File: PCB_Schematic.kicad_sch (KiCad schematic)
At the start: 64 parts, among them J1 IMU_1, J2 Power_Connector, J3 Programming Header, J4 Conn_01x02_Pin, J6 USB_A, J7 Ultrasonic, J8 IMU_2, Q7 BSS138, SW1 Reset Switch, U1 MAX7375AXR805, U2 LM1117MP-ADJ, U3 TPS54331-Q1, U5 FT232RL, U6 STM32F091RCTx

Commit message: minor footprint changes
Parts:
- J2: footprint (none) -> Library:CONN_B4B-XH-A_JSTProject
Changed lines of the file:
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@@
 			)
 		)
-		(property "Footprint" ""
+		(property "Footprint" "Library:CONN_B4B-XH-A_JSTProject"
 			(at 267.97 88.9 0)
 			(effects

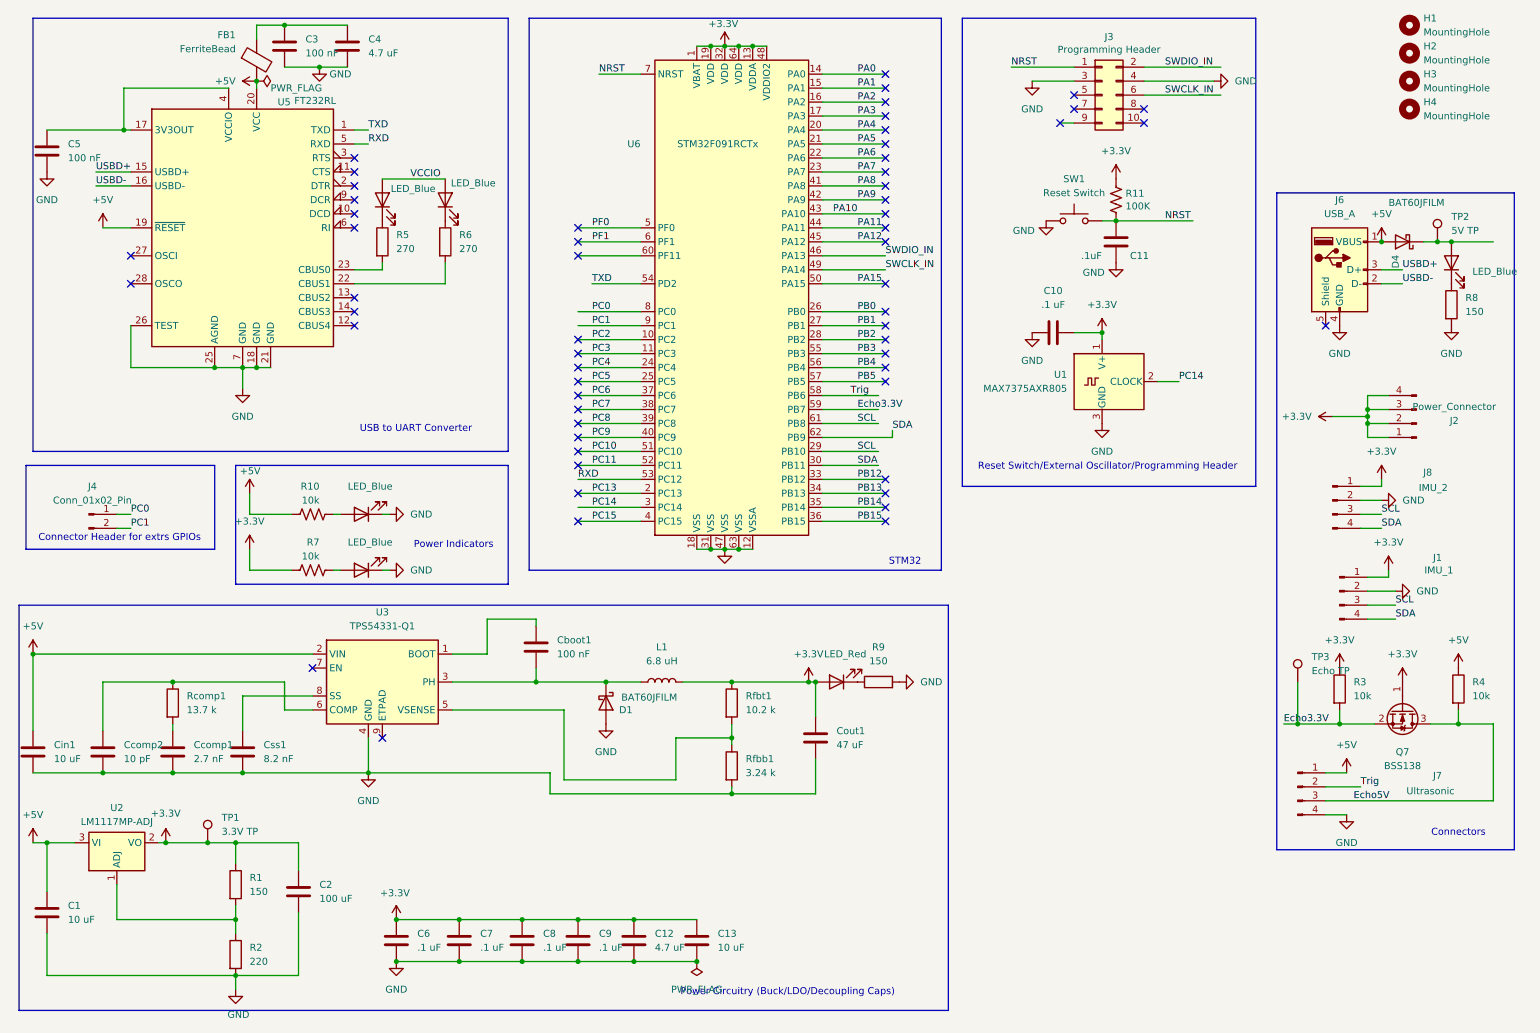
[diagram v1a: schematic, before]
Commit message: OSC_IN pin change, add BOOT0, just copy programming header from schematic
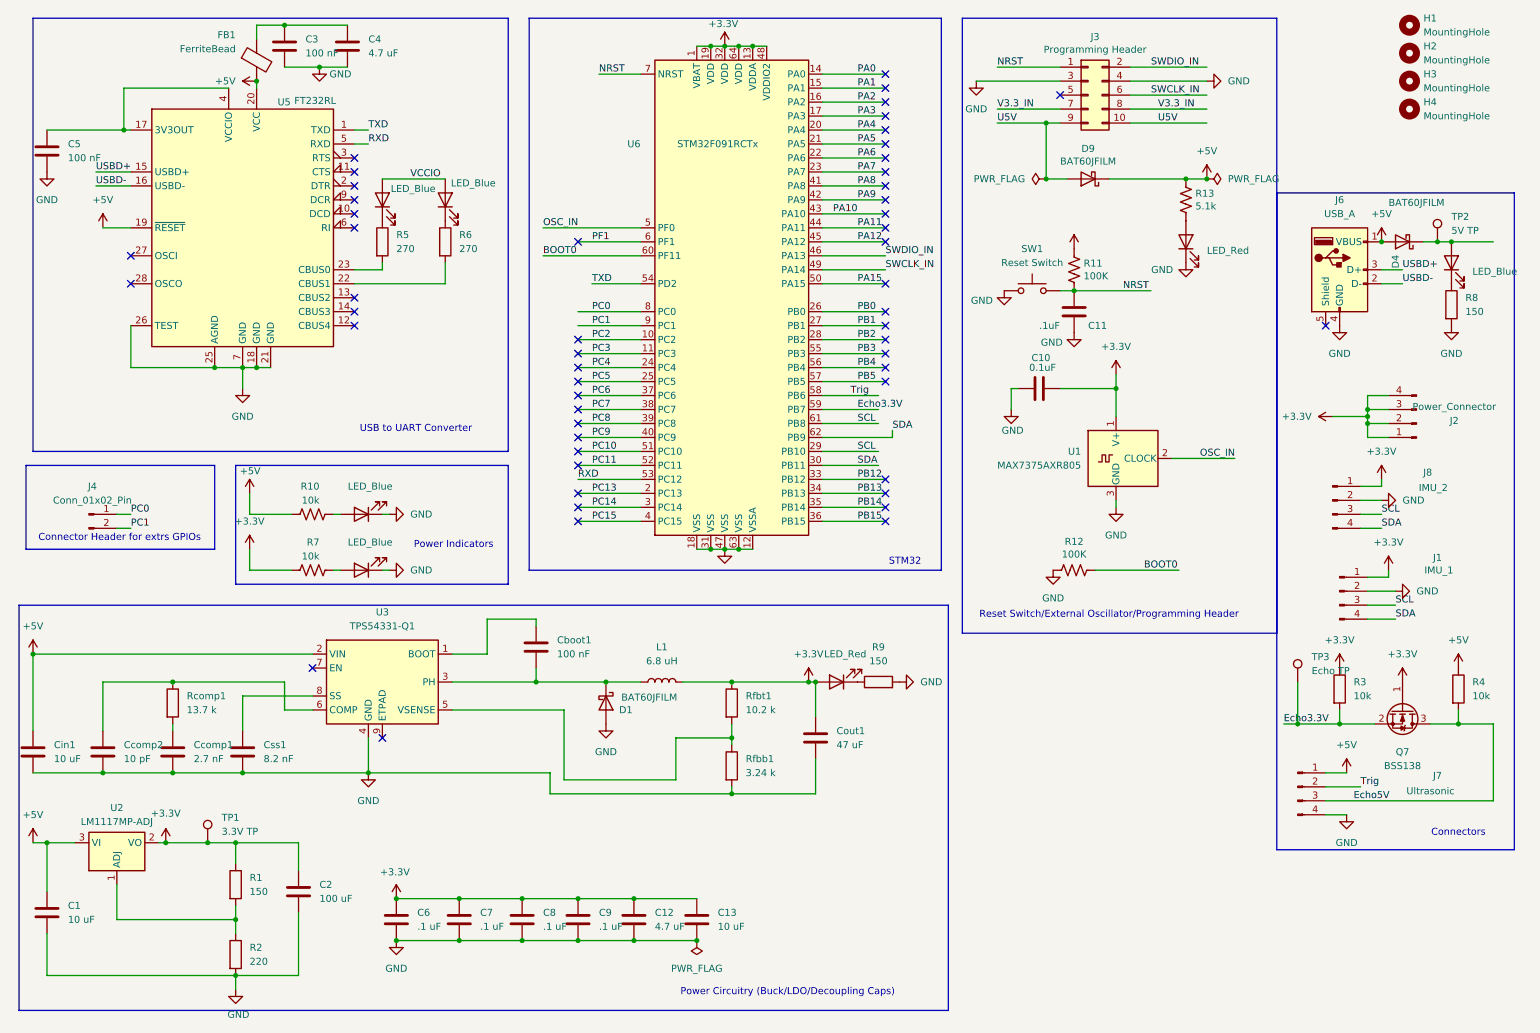
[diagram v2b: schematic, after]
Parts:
- added D10: LED_Red, LED_SMD:LED_0805_2012Metric_Pad1.15x1.40mm_HandSolder, symbol Device:LED
- added D9: BAT60JFILM, Diode_SMD:D_0805_2012Metric_Pad1.15x1.40mm_HandSolder, symbol Diode:BAT60A
- added R12: 100K, Resistor_SMD:R_0805_2012Metric_Pad1.20x1.40mm_HandSolder, symbol Device:R_US
- added R13: 5.1k, Resistor_SMD:R_0805_2012Metric_Pad1.20x1.40mm_HandSolder, symbol Device:R_US
- C10: value .1 uF -> 0.1uF
- U1: footprint Package_TO_SOT_SMD:SOT-323_SC-70 -> Package_TO_SOT_SMD:SOT-323_SC-70_Handsoldering
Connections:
- net +3.3V: now also C10.2; no longer C10.1
- net +5V: now also D9.1 (K), R13.1
- net GND: now also C10.1, D10.1 (K), R12.2; no longer C10.2
- net PC14: no longer U1.2 (CLOCK)
- net BOOT0: now reaches U6.60 (PF11)
- net BOOT0: now also R12.1
- net U5V: now reaches J3.10 (Pin_10)
- net U5V: now also J3.9 (Pin_9), D9.2 (A)
- net V3.3_IN: now reaches J3.7 (Pin_7)
- net V3.3_IN: now also J3.8 (Pin_8)
- net PF0 renamed OSC_IN
- net OSC_IN: now also U1.2 (CLOCK)
- new net: D10.2 (A), R13.2
- no-connect marks 58 -> 53
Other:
- moved on the sheet: C11, C12, C13, C6, C7, C8, C9, R11, SW1

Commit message: new ESD and footprints
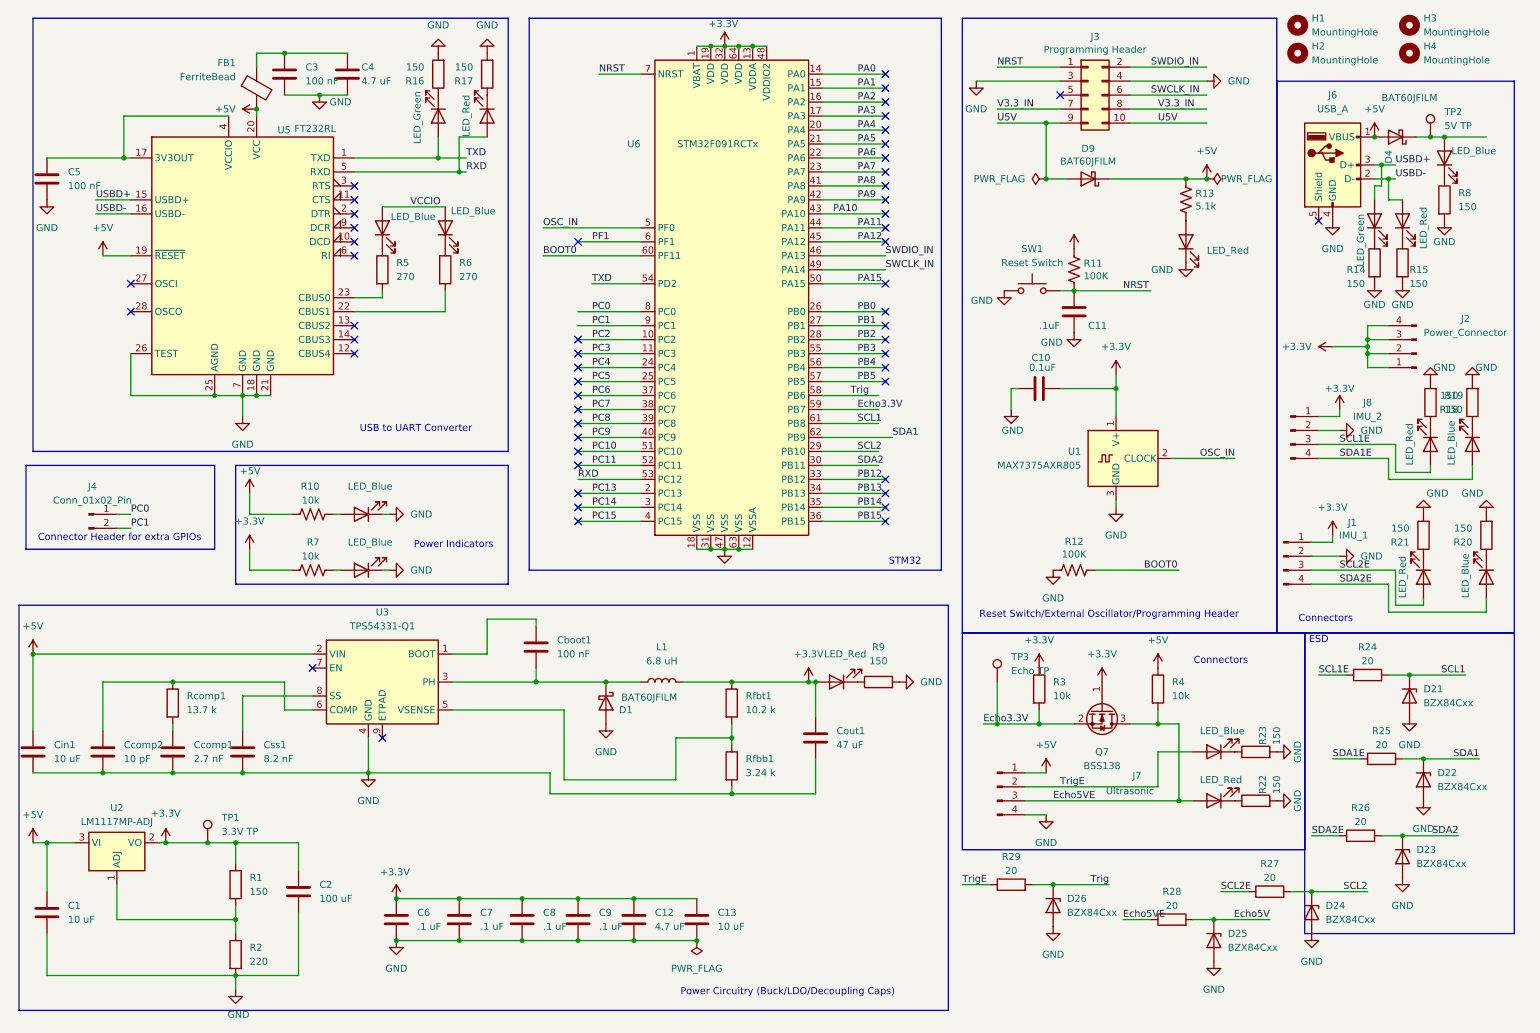
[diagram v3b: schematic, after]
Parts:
- added D11, D13: LED_Green, LED_SMD:LED_0805_2012Metric_Pad1.15x1.40mm_HandSolder, symbol Device:LED
- added D12, D14, D16, D18, D19: LED_Red, LED_SMD:LED_0805_2012Metric_Pad1.15x1.40mm_HandSolder, symbol Device:LED
- added D15, D17, D20: LED_Blue, LED_SMD:LED_0805_2012Metric_Pad1.15x1.40mm_HandSolder, symbol Device:LED
- added D21, D22, D23, D24, D25, D26: BZX84Cxx, Package_TO_SOT_SMD:SOT-23, symbol Diode:BZX84Cxx
- added R14, R15, R16, R17, R18, R19, R20, R21, R22, R23: 150, Resistor_SMD:R_0805_2012Metric_Pad1.20x1.40mm_HandSolder, symbol Device:R
- added R24, R25, R26, R27, R28, R29: 20, Resistor_SMD:R_0805_2012Metric_Pad1.20x1.40mm_HandSolder, symbol Device:R
- J6: footprint (none) -> Library:Project_USB
- Q7: footprint Package_TO_SOT_SMD:SOT-23 -> Library:Project_BSS
- U2: footprint Package_TO_SOT_SMD:SOT-223-3_TabPin2 -> Library:Project_LM1117
- U3: footprint Package_SO:TI_SO-PowerPAD-8_ThermalVias -> Library:Project_TPS
- U5: footprint Package_SO:SSOP-28_5.3x10.2mm_P0.65mm -> Library:Project_FT232
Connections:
- net Echo5V: now also D25.3 (K), R28.2; no longer J7.3 (Pin_3), Q7.3 (D), R4.2
- net GND: now also D21.1 (A), D22.1 (A), D23.1 (A), D24.1 (A), D25.1 (A), D26.1 (A), R14.2, R15.2, R16.2, R17.2, R18.2, R19.2, R20.2, R21.2, R22.2, R23.2
- net RXD: now also D14.2 (A)
- net TXD: now also D13.2 (A)
- net Trig: now also D26.3 (K), R29.2; no longer J7.2 (Pin_2)
- net USBD+: now also D11.2 (A)
- net USBD-: now also D12.2 (A)
- removed net SCL: J1.3 (Pin_3), J8.3 (Pin_3), U6.29 (PB10), U6.61 (PB8)
- removed net SDA: J1.4 (Pin_4), J8.4 (Pin_4), U6.30 (PB11), U6.62 (PB9)
- new net: D19.1 (K), R22.1
- new net: D16.1 (K), R19.1
- new net: D12.1 (K), R15.1
- new net: D11.1 (K), R14.1
- new net: D14.1 (K), R17.1
- new net: D15.1 (K), R18.1
- new net: D18.1 (K), R21.1
- new net: D20.1 (K), R23.1
- new net: D17.1 (K), R20.1
- new net: D13.1 (K), R16.1
- new net Echo5VE: D19.2 (A), J7.3 (Pin_3), Q7.3 (D), R28.1, R4.2
- new net SCL1: D21.3 (K), R24.2, U6.61 (PB8)
- new net SCL1E: D16.2 (A), J8.3 (Pin_3), R24.1
- new net SCL2: D24.3 (K), R27.2, U6.29 (PB10)
- new net SCL2E: D18.2 (A), J1.3 (Pin_3), R27.1
- new net SDA1: D22.3 (K), R25.2, U6.62 (PB9)
- new net SDA1E: D15.2 (A), J8.4 (Pin_4), R25.1
- new net SDA2: D23.3 (K), R26.2, U6.30 (PB11)
- new net SDA2E: D17.2 (A), J1.4 (Pin_4), R26.1
- new net TrigE: D20.2 (A), J7.2 (Pin_2), R29.1
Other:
- note added: "Connector Header for extra GPIOs"
- note added: "ESD"
- note removed: "Connector Header for extrs GPIOs"
- moved on the sheet: C3, C4, C5, D4, FB1, H1, H2, H3, H4, J1, J2, J6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

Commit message: subsheets added
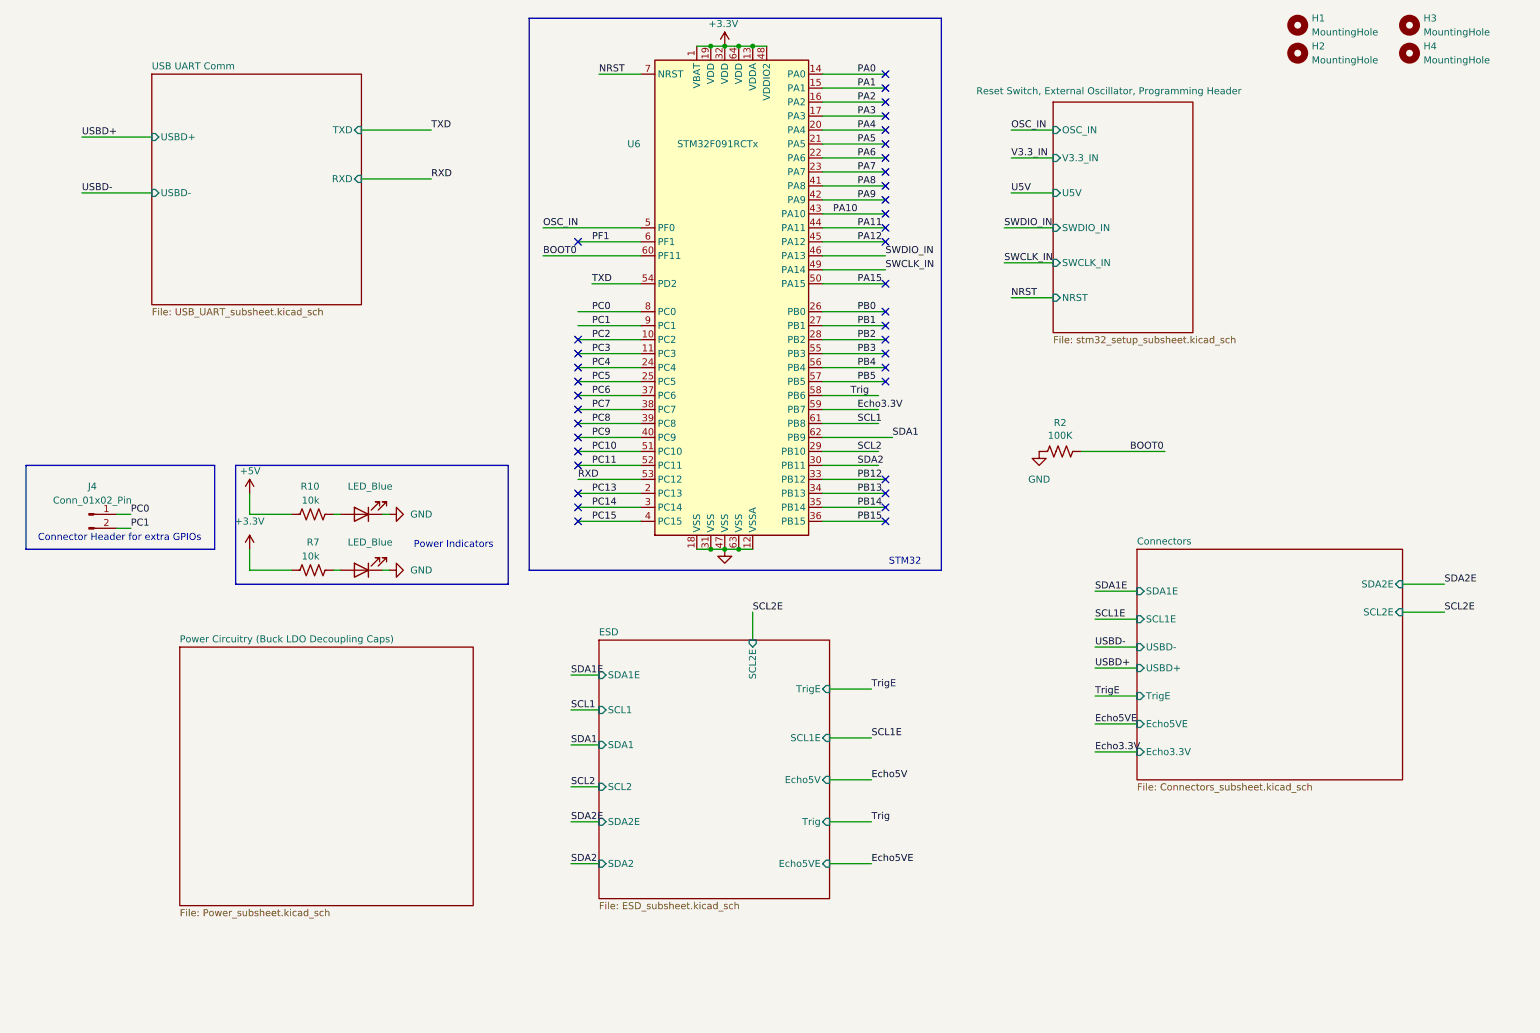
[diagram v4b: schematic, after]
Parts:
- removed C1: 10 uF, symbol Device:C
- removed C10: 0.1uF, Capacitor_SMD:C_0805_2012Metric_Pad1.18x1.45mm_HandSolder, symbol Device:C
- removed C11: .1uF, Capacitor_SMD:C_0805_2012Metric_Pad1.18x1.45mm_HandSolder, symbol Device:C
- removed C12, C4: 4.7 uF, Capacitor_SMD:C_0805_2012Metric_Pad1.18x1.45mm_HandSolder, symbol Device:C
- removed C13, Cin1: 10 uF, Capacitor_SMD:C_0805_2012Metric_Pad1.18x1.45mm_HandSolder, symbol Device:C
- removed C2: 100 uF, symbol Device:C
- removed C3, C5, Cboot1: 100 nF, Capacitor_SMD:C_0805_2012Metric_Pad1.18x1.45mm_HandSolder, symbol Device:C
- removed C6, C7, C8, C9: .1 uF, Capacitor_SMD:C_0805_2012Metric_Pad1.18x1.45mm_HandSolder, symbol Device:C
- removed Ccomp1: 2.7 nF, Capacitor_SMD:C_0805_2012Metric_Pad1.18x1.45mm_HandSolder, symbol Device:C
- removed Ccomp2: 10 pF, Capacitor_SMD:C_0805_2012Metric_Pad1.18x1.45mm_HandSolder, symbol Device:C
- removed Cout1: 47 uF, Capacitor_SMD:C_0805_2012Metric_Pad1.18x1.45mm_HandSolder, symbol Device:C
- removed Css1: 8.2 nF, Capacitor_SMD:C_0805_2012Metric_Pad1.18x1.45mm_HandSolder, symbol Device:C
- removed D1, D4: BAT60JFILM, Diode_SMD:D_0805_2012Metric_Pad1.15x1.40mm_HandSolder, symbol Device:D_Schottky
- removed D10, D12, D14, D16, D18, D19, D7: LED_Red, LED_SMD:LED_0805_2012Metric_Pad1.15x1.40mm_HandSolder, symbol Device:LED
- removed D11, D13: LED_Green, LED_SMD:LED_0805_2012Metric_Pad1.15x1.40mm_HandSolder, symbol Device:LED
- removed D15, D17, D2, D20, D3, D8: LED_Blue, LED_SMD:LED_0805_2012Metric_Pad1.15x1.40mm_HandSolder, symbol Device:LED
- removed D21, D22, D23, D24, D25, D26: BZX84Cxx, Package_TO_SOT_SMD:SOT-23, symbol Diode:BZX84Cxx
- removed D9: BAT60JFILM, Diode_SMD:D_0805_2012Metric_Pad1.15x1.40mm_HandSolder, symbol Diode:BAT60A
- removed FB1: FerriteBead, Inductor_SMD:L_0201_0603Metric_Pad0.64x0.40mm_HandSolder, symbol Device:FerriteBead
- removed J1: IMU_1, Library:CONN_B4B-XH-A_JSTProject, symbol Connector:Conn_01x04_Pin
- removed J2: Power_Connector, Library:CONN_B4B-XH-A_JSTProject, symbol Connector:Conn_01x04_Pin
- removed J3: Programming Header, Connector_IDC:IDC-Header_2x05_P2.54mm_Vertical, symbol Connector_Generic:Conn_02x05_Odd_Even
- removed J6: USB_A, Library:Project_USB, symbol Connector:USB_A
- removed J7: Ultrasonic, Library:CONN_B4B-XH-A_JSTProject, symbol Connector:Conn_01x04_Pin
- removed J8: IMU_2, Library:CONN_B4B-XH-A_JSTProject, symbol Connector:Conn_01x04_Pin
- removed L1: 6.8 uH, Inductor_SMD:L_0805_2012Metric_Pad1.15x1.40mm_HandSolder, symbol Device:L
- removed Q7: BSS138, Library:Project_BSS, symbol Transistor_FET:BSS138
- removed R1, R14, R15, R16, R17, R18, R19, R20, R21, R22, R23, R8, R9: 150, Resistor_SMD:R_0805_2012Metric_Pad1.20x1.40mm_HandSolder, symbol Device:R
- removed R11, R12: 100K, Resistor_SMD:R_0805_2012Metric_Pad1.20x1.40mm_HandSolder, symbol Device:R_US
- removed R13: 5.1k, Resistor_SMD:R_0805_2012Metric_Pad1.20x1.40mm_HandSolder, symbol Device:R_US
- removed R2: 220, Resistor_SMD:R_0805_2012Metric_Pad1.20x1.40mm_HandSolder, symbol Device:R
- removed R24, R25, R26, R27, R28, R29: 20, Resistor_SMD:R_0805_2012Metric_Pad1.20x1.40mm_HandSolder, symbol Device:R
- removed R3, R4: 10k, Resistor_SMD:R_0805_2012Metric_Pad1.20x1.40mm_HandSolder, symbol Device:R
- removed R5: 270, Resistor_SMD:R_0805_2012Metric_Pad1.20x1.40mm_HandSolder, symbol Device:R
- removed R6: 270, Capacitor_SMD:C_0805_2012Metric_Pad1.18x1.45mm_HandSolder, symbol Device:R
- removed Rcomp1: 13.7 k, Resistor_SMD:R_0805_2012Metric_Pad1.20x1.40mm_HandSolder, symbol Device:R
- removed Rfbb1: 3.24 k, Resistor_SMD:R_0805_2012Metric_Pad1.20x1.40mm_HandSolder, symbol Device:R
- removed Rfbt1: 10.2 k, Resistor_SMD:R_0805_2012Metric_Pad1.20x1.40mm_HandSolder, symbol Device:R
- removed SW1: Reset Switch, Button_Switch_SMD:SW_SPST_PTS645, symbol Switch:SW_Push
- removed TP1: 3.3V TP, TestPoint:TestPoint_Loop_D3.50mm_Drill1.4mm_Beaded, symbol Connector:TestPoint
- removed TP2: 5V TP, TestPoint:TestPoint_Loop_D3.50mm_Drill1.4mm_Beaded, symbol Connector:TestPoint
- removed TP3: Echo TP, TestPoint:TestPoint_Loop_D3.50mm_Drill1.4mm_Beaded, symbol Connector:TestPoint
- removed U1: MAX7375AXR805, Package_TO_SOT_SMD:SOT-323_SC-70_Handsoldering, symbol Oscillator:MAX7375AXR805
- removed U2: LM1117MP-ADJ, Library:Project_LM1117, symbol Regulator_Linear:LM1117MP-ADJ
- removed U3: TPS54331-Q1, Library:Project_TPS, symbol Regulator_Switching:TPS54336ADDA
- removed U5: FT232RL, Library:Project_FT232, symbol Interface_USB:FT232RL
- added R2: 100K, Resistor_SMD:R_0805_2012Metric_Pad1.20x1.40mm_HandSolder, symbol Device:R_US
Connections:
- net BOOT0: now also R2.1
- net GND: now also R2.2
- no-connect marks 53 -> 38
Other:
- added sheet Connectors (Connectors_subsheet.kicad_sch)
- added sheet ESD (ESD_subsheet.kicad_sch)
- added sheet Power Circuitry (Buck LDO Decoupling Caps) (Power_subsheet.kicad_sch)
- added sheet Reset Switch, External Oscillator, Programming Header (stm32_setup_subsheet.kicad_sch)
- added sheet USB UART Comm (USB_UART_subsheet.kicad_sch)
- note removed: "Connectors"
- note removed: "ESD"
- note removed: "Power Circuitry (Buck/LDO/Decoupling Caps)"
- note removed: "Reset Switch/External Oscillator/Programming Header"
- note removed: "USB to UART Converter"
